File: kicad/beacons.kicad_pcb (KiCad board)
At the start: 2 copper layers, 151.3 x 106.7 mm, 81 parts, among them IC1 AP7179DSKZ20-13, IC2 AP7179DSKZ20-13, IC3 PN7160A1HN_C100E, J1 USB_C_Receptacle_USB2.0_16P, J2 Conn_01x03, J3 Conn_01x18, J4 Conn_01x02, J5 Conn_01x07, J6 Conn_01x07, SW1 SW_Push, SW2 SW_Push, SW3 SW_SPST, U1 ESP32-S3-WROOM-1, U2 SN74LVC1T45DCK, U3 74HC595, U4 MAX17048G+T10, U5 MCP73831-2-OT, Y1 27.12MHz Crystal

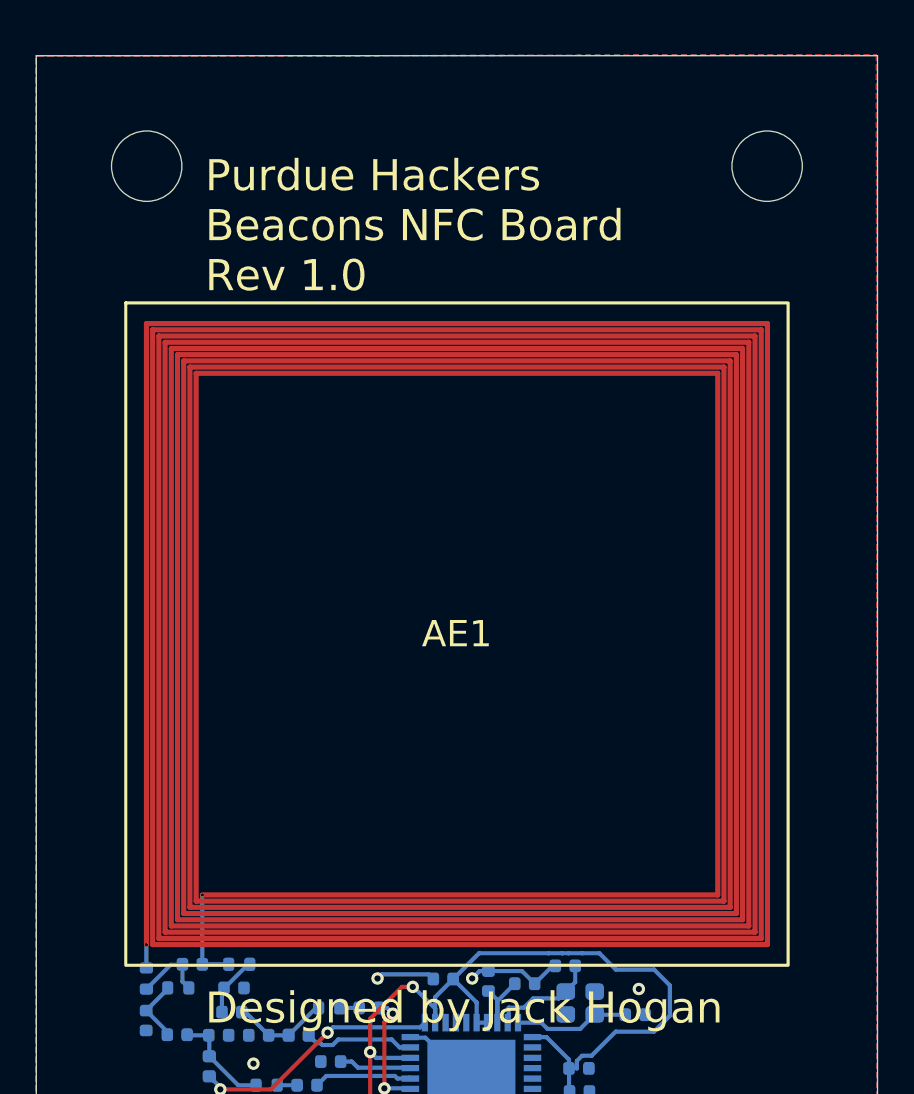
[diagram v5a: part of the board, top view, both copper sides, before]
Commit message: Move nfc antenna away from traces
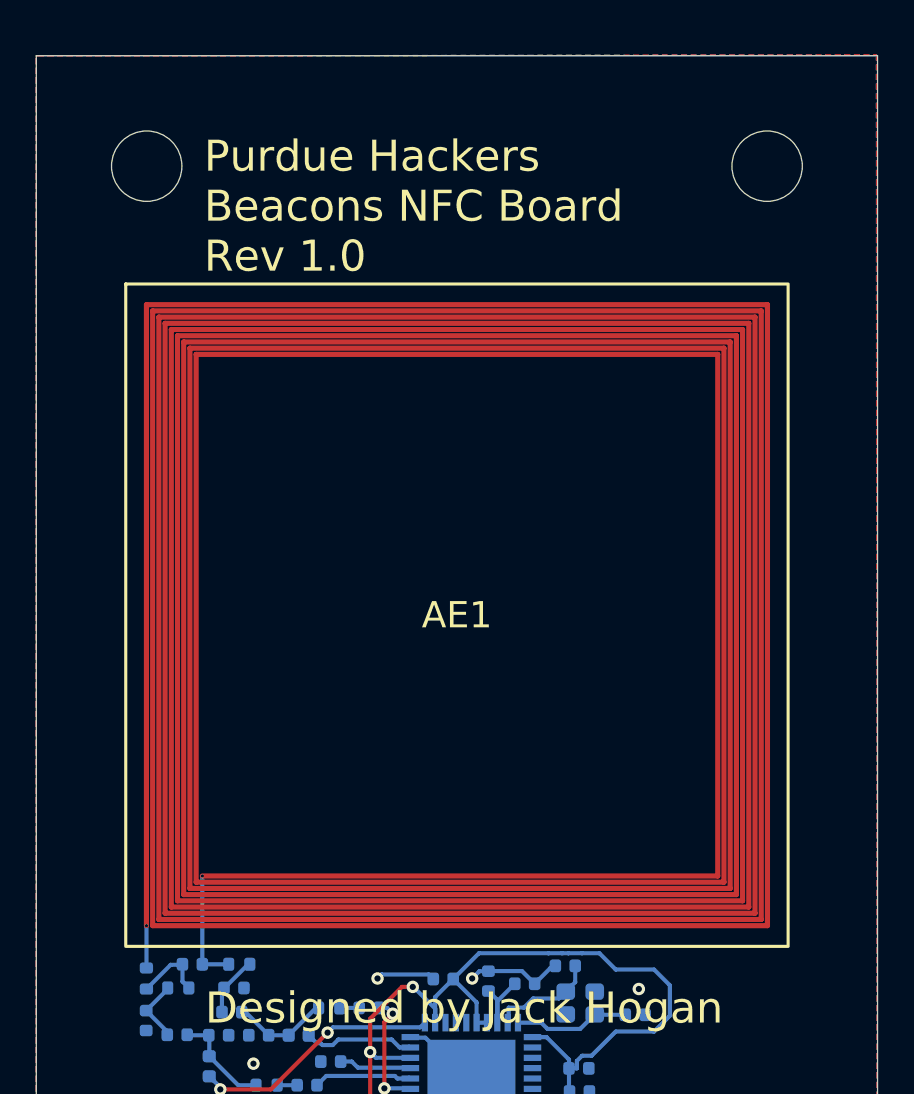
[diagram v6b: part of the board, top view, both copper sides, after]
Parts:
- moved AE1 0.91 mm to (204.6, 82.7)
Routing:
- net Net-(AE1-Pad1): track 1.13 -> 2.04 mm
- net Net-(AE1-Pad2): track 4.65 -> 5.54 mm
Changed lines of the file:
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@@
 	(footprint "footprints:NFC"
 		(layer "F.Cu")
-		(at 204.598197 83.6422)
+		(at 204.598197 82.7278)
 		(property "Reference" "AE1"
 			(at 0 0 0)
@@
 	)
 	(gr_text "Purdue Hackers\nBeacons NFC Board\nRev 1.0"
-		(at 192.4304 67.2084 0)
+		(at 192.3796 66.2686 0)
 		(layer "F.SilkS")
 		(effects
@@
 	)
 	(segment
-		(start 192.2982 96.242198)
-		(end 192.2982 99.6188)
+		(start 193.5714 99.5934)
+		(end 192.2982 99.5934)
 		(width 0.2)
 		(layer "B.Cu")
@@
 	)
 	(segment
-		(start 193.5714 99.5934)
-		(end 192.2982 99.5934)
+		(start 192.2982 99.5934)
+		(end 192.2982 95.327798)
 		(width 0.2)
 		(layer "B.Cu")
@@
 	)
 	(segment
-		(start 189.597 98.6422)
-		(end 189.597 99.7712)
+		(start 189.597 97.728997)
+		(end 189.598197 97.7278)
+		(width 0.2)
+		(layer "B.Cu")
+		(net 88)
+	)
+	(segment
+		(start 189.597 99.7712)
+		(end 189.597 97.728997)
 		(width 0.2)
 		(layer "B.Cu")
@@
 		(filled_areas_thickness no)
 		(keepout
-			(tracks allowed)
-			(vias allowed)
-			(pads allowed)
+			(tracks not_allowed)
+			(vias not_allowed)
+			(pads not_allowed)
 			(copperpour not_allowed)
-			(footprints allowed)
+			(footprints not_allowed)
 		)
 		(placement
@@
 		(polygon
 			(pts
-				(xy 220.5736 67.6402) (xy 220.6752 99.6696) (xy 188.5188 99.6188) (xy 188.5188 67.6402)
+				(xy 220.6752 66.6496) (xy 220.6752 98.806281) (xy 188.5188 98.755481) (xy 188.5188 66.6496)
 			)
 		)

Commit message: Start pcb review
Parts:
- moved C5 3.41 mm to (209.9, 102.6), turned to 90 degrees
- moved C6 1.37 mm to (208.9, 100.7), turned to -90 degrees
- moved Y1 1.32 mm to (211.2, 100.3)
- moved C10 0.72 mm to (207.2, 100.4), turned to 90 degrees
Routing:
- net /NFC/NFC_GND: track 14.9 -> 24.0 mm, vias 6 -> 26
- net /I2C_SDA: track 145.9 -> 154.5 mm
- net /REG_POS: track 23.6 -> 28.6 mm
- net /S1: track 42.9 -> 38.8 mm
- net +5V: track 183.8 -> 181.0 mm, vias 2 -> 1
- net /LED_PEAK: track 84.0 -> 81.4 mm
- net /NFC/NFC_3V3: track 63.5 -> 65.9 mm
- net /NFC_EN: track 109.8 -> 111.9 mm
- net /NFC_FWUD: track 97.5 -> 99.1 mm
- net /NFC_IRQ: track 105.5 -> 107.0 mm
- net /SPI_CLK: track 115.6 -> 114.2 mm
- net /USB_NEG: track 39.8 -> 38.4 mm
- net GND: track 13.3 -> 14.5 mm, vias 6 -> 143
- net /S0: track 42.8 -> 43.9 mm
- net /NFC/I2C_SDA: track 6.97 -> 6.41 mm
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- added copper zone on B.Cu, net /NFC/NFC_3V3
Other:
- board text added: "im straight up :jack:ing it and by it uhm uhh lest jusr say my pcb"
